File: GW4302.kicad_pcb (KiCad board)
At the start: 4 copper layers, 57.9 x 60.3 mm, 74 parts, among them J1 C64, J2 microUSB, J3 JTAG, U1 74AHC245PW, U10 74AHC125PW, U13 CH340G, U2 74AHC245PW, U3 LD1117S33, U4 74AHC245PW, U5 74AHC245PW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

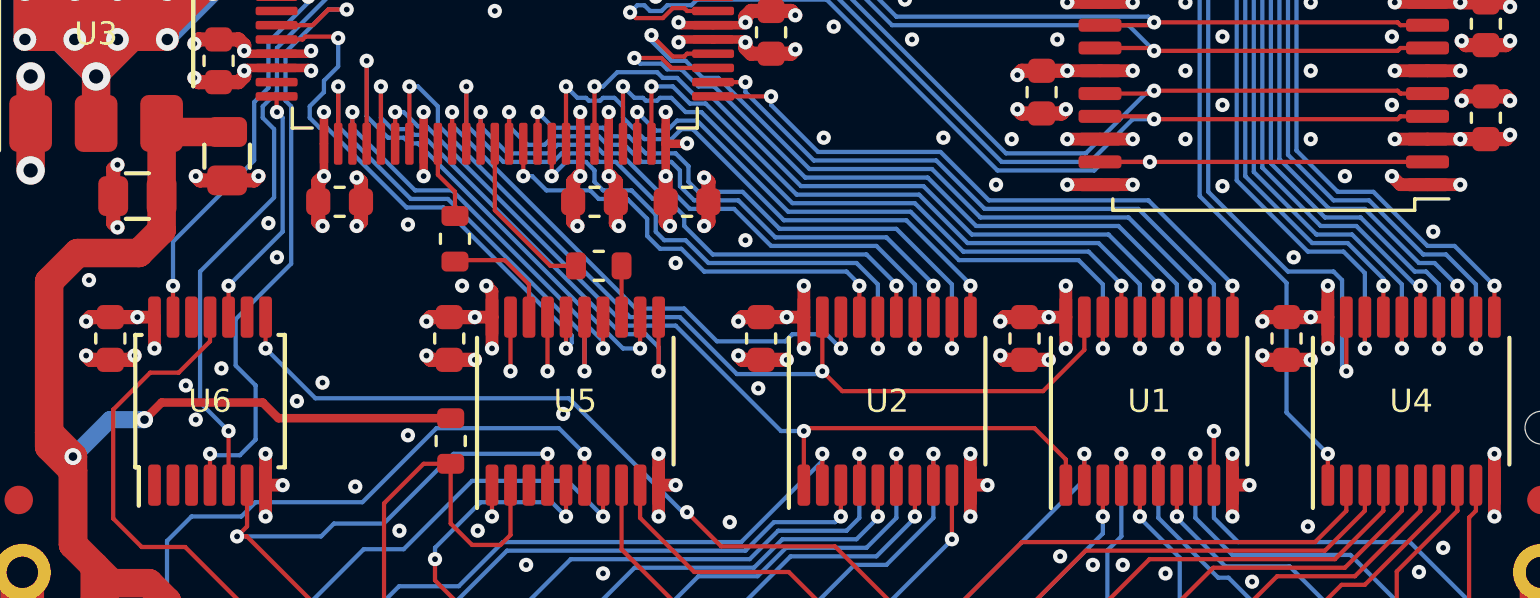
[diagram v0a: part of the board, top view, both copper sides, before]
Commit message: Add pull-up resistors on AOE, DOE, IRQOE, RESOE
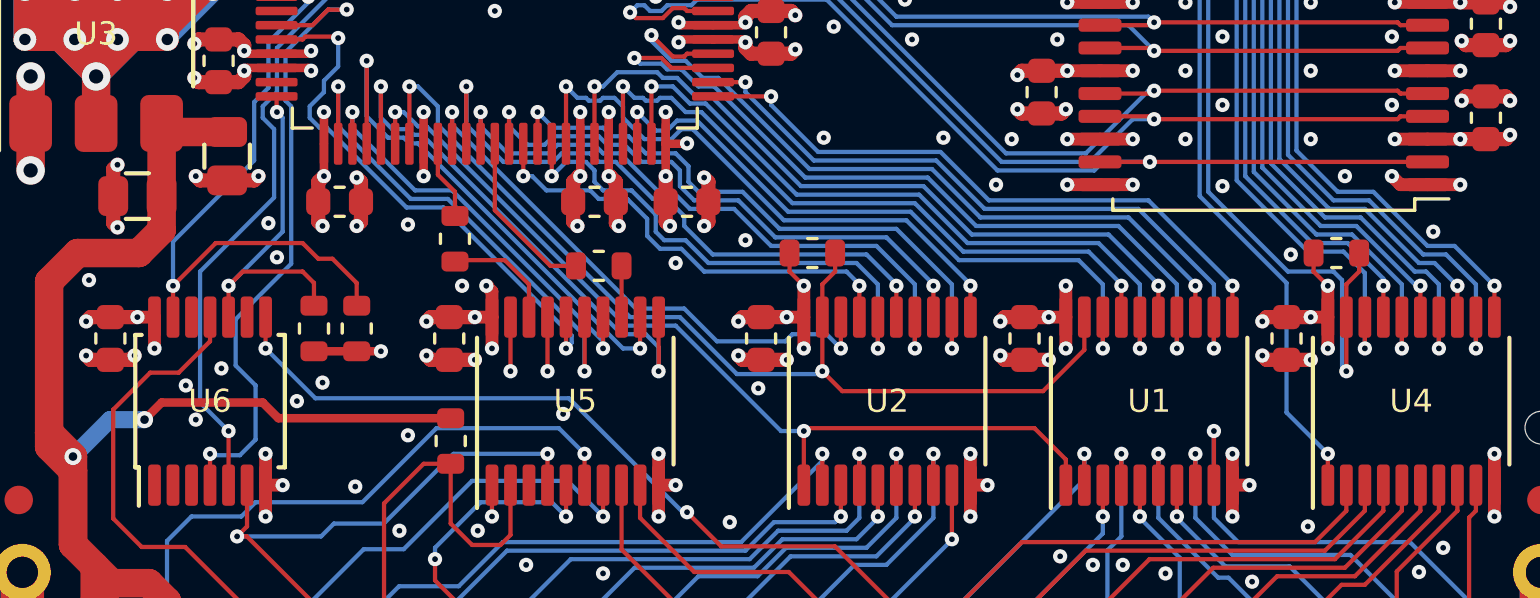
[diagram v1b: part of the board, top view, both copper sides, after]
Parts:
- added R17: 1k, stdpads:R_0603, F.Cu at (133.2, 76.8)
- added R18: 1k, stdpads:R_0603, F.Cu at (117.2, 79.5)
- added R19: 1k, stdpads:R_0603, F.Cu at (151.6, 76.8)
- added R20: 1k, stdpads:R_0603, F.Cu at (115.7, 79.5)
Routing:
- net /IRQ~{OE}: track 14.3 -> 22.8 mm
- net +3V3: track 381.1 -> 386.2 mm, vias 115 -> 116
- net /DMA~{OE}: track 8.63 -> 12.8 mm
- net /D~{OE}: track 56.0 -> 58.5 mm
- net /A~{OE}: track 34.3 -> 36.7 mm

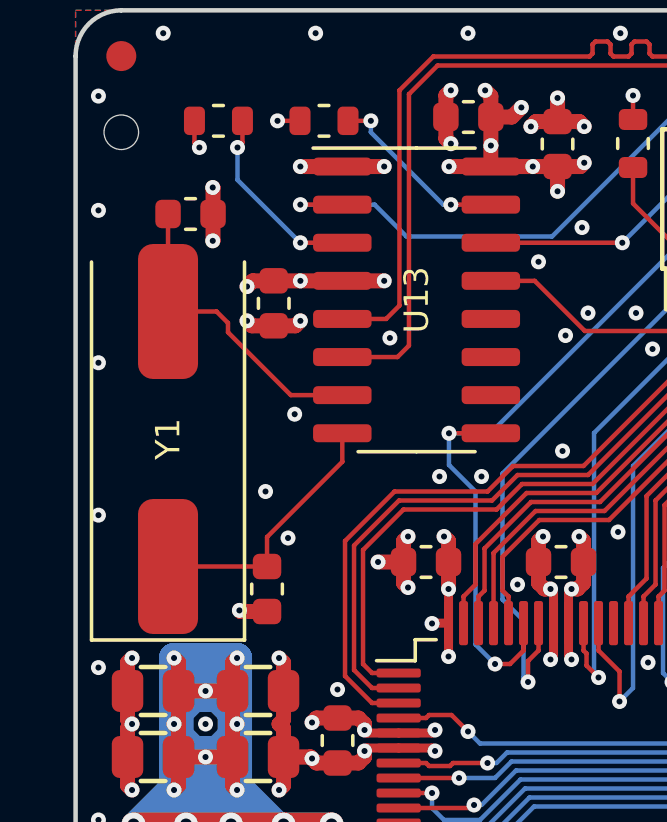
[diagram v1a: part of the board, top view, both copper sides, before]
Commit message: Switch to 3225 crystal for USB
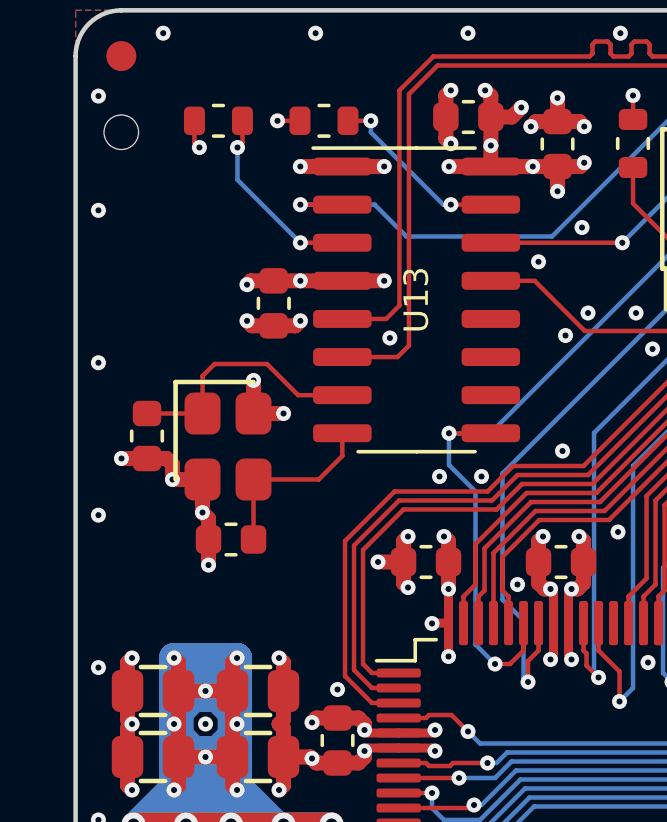
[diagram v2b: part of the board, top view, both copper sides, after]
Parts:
- Y1: footprint stdpads:Crystal_HC49-SMD -> stdpads:Crystal_SMD_3225-4Pin_3.2x2.5mm
- moved C33 7.54 mm to (106.0, 51.4), turned to -90 degrees
- moved C32 2.04 mm to (108.8, 54.9), turned to 180 degrees
- moved Y1 2.02 mm to (108.7, 51.8), turned to -90 degrees
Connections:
- Y1 pad 1: Net-(C32-Pad1) -> Net-(C33-Pad1)
- Y1 pad 2: Net-(C33-Pad1) -> GND
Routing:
- net GND: track 158.7 -> 164.3 mm
- net Net-(C32-Pad1): track 8.78 -> 6.04 mm
- net Net-(C33-Pad1): track 10.4 -> 8.36 mm

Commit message: Fix board ID
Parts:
- added D1: LED, stdpads:LED_0805, F.Cu at (145.7, 40.8)
- added R21: 1k, stdpads:R_0603, F.Cu at (116.4, 83.8)
- added R22: 220, stdpads:R_0805, F.Cu at (147.8, 40.8)
- added R23: 1k, stdpads:R_0603, F.Cu at (109.8, 57.9)
- moved R4 3.48 mm to (109.8, 44.0), turned to -90 degrees
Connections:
- U13 pad 10: unconnected-(U13-Pad10) -> Net-(U13-Pad10)
- U13 pad 11: unconnected-(U13-Pad11) -> Net-(U13-Pad10)
- U13 pad 12: unconnected-(U13-Pad12) -> Net-(U13-Pad10)
- U8 pad 24: unconnected-(U8-Pad24) -> /~{LED}
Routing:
- net /~{LED}: track 0.00 -> 94.0 mm, vias 0 -> 2
- net Net-(U13-Pad10): track 0.00 -> 19.4 mm
- net /RW~{OE}: track 23.2 -> 26.9 mm, vias 2 -> 3
- net Net-(R4-Pad2): track 6.40 -> 2.70 mm, vias 2 -> 1
- net Net-(D1-Pad2): track 0.00 -> 2.16 mm
- net +3V3: track 386.1 -> 387.9 mm, vias 116 -> 117
